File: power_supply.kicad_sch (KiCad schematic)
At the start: 23 parts, among them J1 USB_C_Receptacle_USB2.0_16P, J2 LDO_SEL, J3 J_LED_VBUS, J4 J_LED_3V3, J5 J_IMEAS, J7 J_EXT_PWR, U1 AP2112K-3.3, U2 MCP1700x-330xxTT, U3 USB_ESD

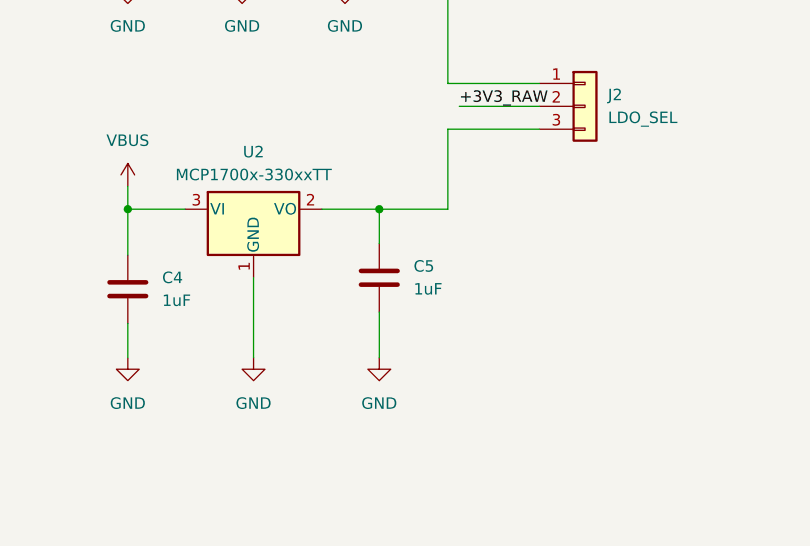
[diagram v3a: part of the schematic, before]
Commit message: Created PCB editor, configure for JLCPCB standards
Additionally, created a specific library for castellard jumpers
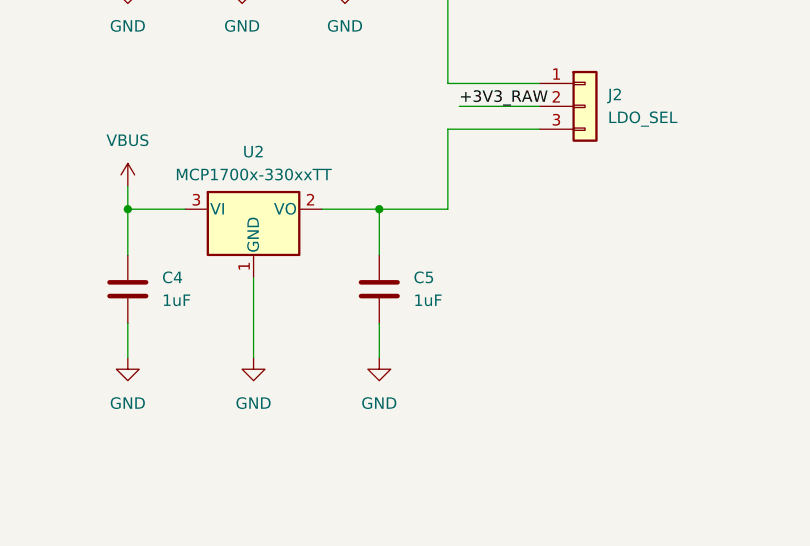
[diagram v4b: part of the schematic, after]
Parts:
- C4, C5: footprint (none) -> Capacitor_SMD:C_0603_1608Metric_Pad1.08x0.95mm_HandSolder

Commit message: Started PCB placing
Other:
- title: (none) -> ${PROJECT_NAME}, Guillermo Gil
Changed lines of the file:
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@@
 	(generator_version "10.0")
 	(paper "A4")
+	(title_block
+		(title "${PROJECT_NAME}, Guillermo Gil")
+		(rev "v.0.1")
+	)
 	(junction
 		(at 71.12 81.28)

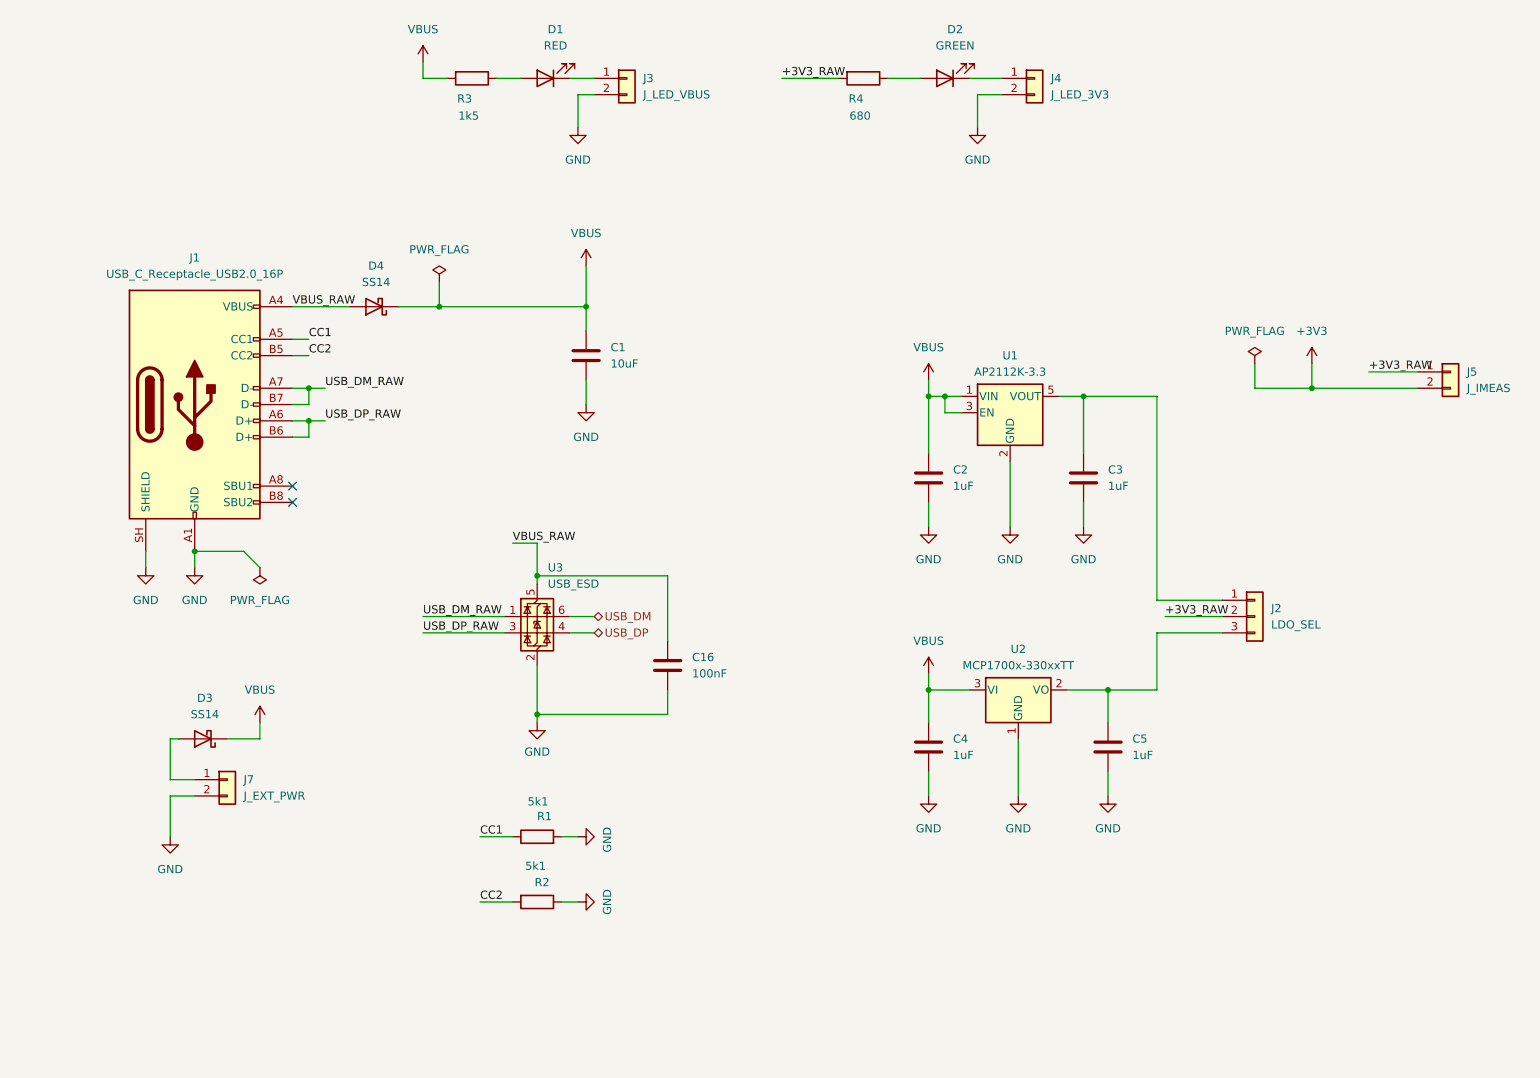
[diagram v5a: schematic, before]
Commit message: v0.2: low-power redesign — single LDO, ideal diodes, LSE, castellated SWD
Power supply:
- Replace dual LDO (AP2112K + MCP1700) with single TPS7A0233PDBV
  (25 nA Iq nanopower; EN tied to IN per datasheet)
- Replace SS14 Schottky diodes with LM66100 ideal diode controllers
  in diode-OR configuration (CE tied to VOUT for RCB mode)
- Remove jumpers J2 (LDO_SEL), J3 (LED_VBUS), J4 (LED_3V3)
- Replace JST battery connector with castellated header J_VBAT
- Replace J5 IMEAS jumper with 0R bridge
- Rename diode-OR output net to VDC

MCU:
- Add LSE crystal Y1 (32.768 kHz ABS07) with 18 pF load caps
- Dedicate PC14/PC15 to LSE oscillator (removed from J_R breakout)
- Wire BOOT0 net to PB8 (requires nBOOT_SEL=0 option byte)
- Replace VREF_SEL 3-pin jumper with two 0R bridges
- Change reset/boot buttons to C&K PTS810SJM250SMTR (smaller)
- Remove user button SW3

SWD:
- J6 changed from 1x05 THT to 1x06 castellated header
- Pinout follows ST-Link V2 Mini: 3V3/SWCLK/GND/SWDIO/NRST/SWO
- SWO (PB3) shared with GPIO breakout

GPIO breakout:
- Move PA2/PA3 from J_L to J_R (filling former PC14/PC15 slots)
- Add +3V3 and extra GND to J_L in vacated positions
- Break out PC13 to J_R
- J9 UART connector: SMD hand-solderable, no series resistors

Re-annotate all references for sequential numbering.
ERC: clean (with documented exclusion for diode-OR power outputs).
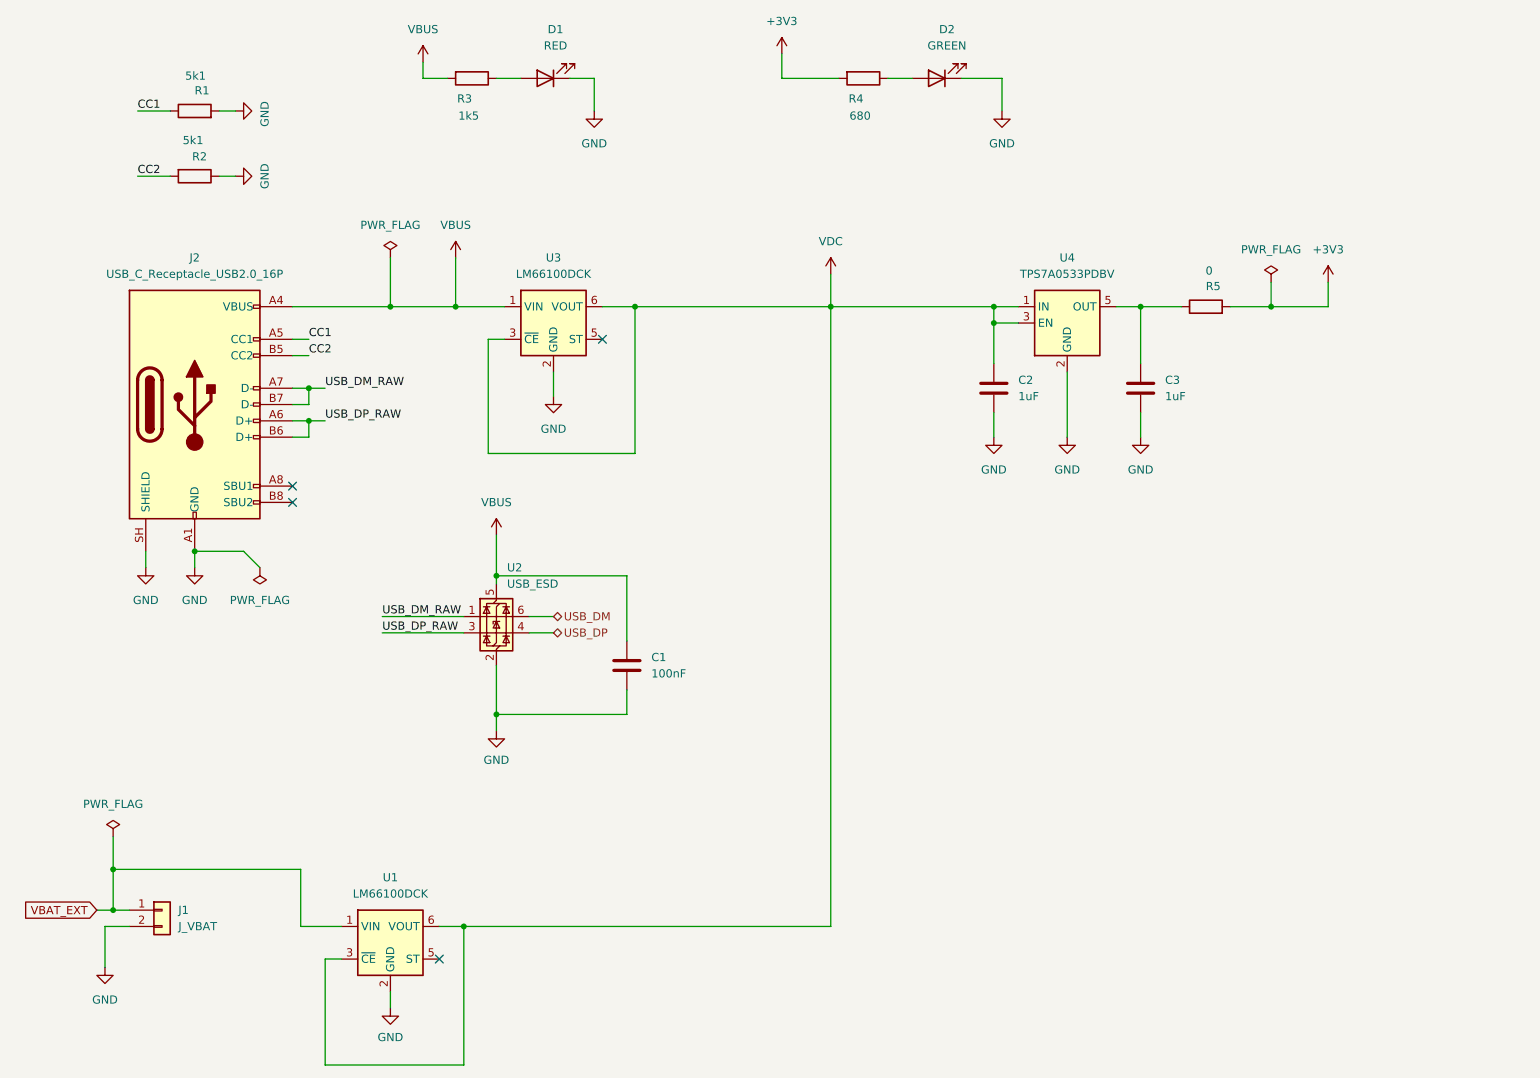
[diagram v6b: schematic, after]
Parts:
- removed C1: 10uF, Capacitor_SMD:C_0603_1608Metric_Pad1.08x0.95mm_HandSolder, symbol Device:C
- removed C4, C5: 1uF, Capacitor_SMD:C_0603_1608Metric_Pad1.08x0.95mm_HandSolder, symbol Device:C
- removed D3, D4: SS14, Diode_SMD:D_SOD-123, symbol Device:D_Schottky
- removed J2: LDO_SEL, Connector_PinHeader_2.54mm:PinHeader_1x03_P2.54mm_Vertical, symbol Connector_Generic:Conn_01x03
- removed J3: J_LED_VBUS, Connector_PinHeader_2.54mm:PinHeader_1x02_P2.54mm_Vertical, symbol Connector_Generic:Conn_01x02
- removed J4: J_LED_3V3, Connector_PinHeader_2.54mm:PinHeader_1x02_P2.54mm_Vertical, symbol Connector_Generic:Conn_01x02
- removed J5: J_IMEAS, Connector_PinHeader_2.54mm:PinHeader_1x02_P2.54mm_Vertical, symbol Connector_Generic:Conn_01x02
- removed J7: J_EXT_PWR, Connector_JST:JST_PH_S2B-PH-K_1x02_P2.00mm_Horizontal, symbol Connector_Generic:Conn_01x02
- removed U1: AP2112K-3.3, Package_TO_SOT_SMD:SOT-23-5_HandSoldering, symbol Regulator_Linear:AP2112K-3.3
- removed U2: MCP1700x-330xxTT, Package_TO_SOT_SMD:SOT-23_Handsoldering, symbol Regulator_Linear:MCP1700x-330xxTT
- added J1: J_VBAT, stm32g431_devboard:PinHeader_1x02_P2.54mm_Vertical_Castellar, symbol Connector_Generic:Conn_01x02
- added R5: 0, Resistor_SMD:R_0603_1608Metric_Pad0.98x0.95mm_HandSolder, symbol Device:R
- added U1, U3: LM66100DCK, Package_TO_SOT_SMD:SOT-363_SC-70-6, symbol Power_Management:LM66100DCK
- added U4: TPS7A0533PDBV, Package_TO_SOT_SMD:SOT-23-5_HandSoldering, symbol Regulator_Linear:TPS7A0533PDBV
- U2: renamed from U3; footprint Package_TO_SOT_SMD:SOT-23-6_Handsoldering -> Package_TO_SOT_SMD:SOT-23-6
- renumbered C16 to C1, J1 to J2
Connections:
- net +3V3_RAW is gone; now on net +3V3: R4.2
- net VBUS_RAW is gone; now on net VBUS: C1.1, J2.A4 (VBUS), J2.A9 (VBUS), J2.B4 (VBUS), J2.B9 (VBUS), U2.5 (VBUS)
- net +3V3: now also R5.2
- net GND: now also D1.1 (K), D2.1 (K), J1.2 (Pin_2), U1.2 (GND), U3.2 (GND), U4.2 (GND)
- net VBUS: now also U3.1 (VIN); no longer C2.1
- net at C3.1: now also R5.1, U4.5 (OUT)
- new net VBAT_EXT: J1.1 (Pin_1), U1.1 (VIN)
- new net VDC: C2.1, U1.3 (~{CE}), U1.6 (VOUT), U3.3 (~{CE}), U3.6 (VOUT), U4.1 (IN), U4.3 (EN)
- no-connect marks 2 -> 4
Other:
- moved on the sheet: C1, C2, C3, D2, R1, R2, U2

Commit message: Finish routing
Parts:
- J1: footprint stm32g431_devboard:PinHeader_1x02_P2.54mm_Vertical_Castellar -> Connector_PinHeader_2.54mm:PinHeader_1x02_P2.54mm_Vertical
- J2: footprint Connector_USB:USB_C_Receptacle_GCT_USB4085 -> stm32g431_devboard:USB_C_Receptacle_GCT_USB4085
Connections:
- net USB_DM renamed USB_N
- net USB_DM_RAW renamed USB_RAW_N
- net USB_DP renamed USB_P
- net USB_DP_RAW renamed USB_RAW_P
